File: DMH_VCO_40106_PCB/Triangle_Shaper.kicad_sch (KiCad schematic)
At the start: 16 parts, among them Q3 BC548, Q4 BC548, U3 TL074, U4 TL074

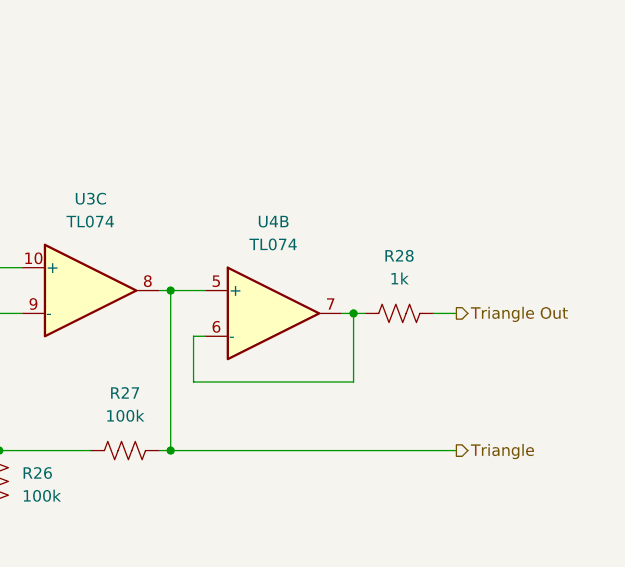
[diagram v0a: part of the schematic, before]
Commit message: Started positioning components on PCB
Moving some input resistores from main PCB to Jacks PCB
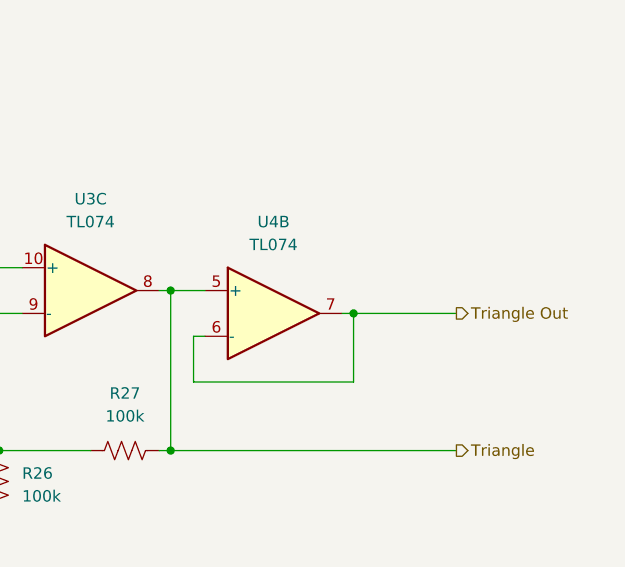
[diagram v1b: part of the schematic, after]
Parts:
- removed R28: 1k, Resistor_THT:R_Axial_DIN0204_L3.6mm_D1.6mm_P5.08mm_Horizontal, symbol Device:R_US
- C12: footprint (none) -> Capacitor_THT:C_Disc_D3.0mm_W2.0mm_P2.50mm
- C13: footprint (none) -> Capacitor_THT:C_Disc_D4.3mm_W1.9mm_P5.00mm
- Q3, Q4: footprint Package_TO_SOT_THT:TO-92_Inline -> Package_TO_SOT_THT:TO-92_Inline_Wide
- R22, R23, R24, R25, R26, R27: footprint Resistor_THT:R_Axial_DIN0204_L3.6mm_D1.6mm_P5.08mm_Horizontal -> Resistor_THT:R_Axial_DIN0207_L6.3mm_D2.5mm_P7.62mm_Horizontal
- TP5, TP6: footprint (none) -> TestPoint:TestPoint_THTPad_2.0x2.0mm_Drill1.0mm; now left out of the parts list
- U4: footprint (none) -> Package_DIP:DIP-14_W7.62mm_Socket
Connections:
- net Triangle Out: now also U4.6 (-), U4.7
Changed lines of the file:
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@@
 	(wire
 		(pts
-			(xy 219.71 99.06) (xy 222.25 99.06)
+			(xy 210.82 99.06) (xy 222.25 99.06)
 		)
 		(stroke
@@
 		)
 	)
-	(wire
-		(pts
-			(xy 210.82 99.06) (xy 212.09 99.06)
-		)
-		(stroke
-			(width 0)
-			(type default)
-		)
-	)
 	(hierarchical_label "Triangle Out"
 		(shape output)
@@
 			)
 		)
-		(property "Footprint" "Resistor_THT:R_Axial_DIN0204_L3.6mm_D1.6mm_P5.08mm_Horizontal"
+		(property "Footprint" "Resistor_THT:R_Axial_DIN0207_L6.3mm_D2.5mm_P7.62mm_Horizontal"
 			(at 143.764 99.314 90)
 			(effects
@@
 			)
 		)
-		(property "Footprint" "Resistor_THT:R_Axial_DIN0204_L3.6mm_D1.6mm_P5.08mm_Horizontal"
+		(property "Footprint" "Resistor_THT:R_Axial_DIN0207_L6.3mm_D2.5mm_P7.62mm_Horizontal"
 			(at 122.936 95.504 90)
 			(effects
@@
 			)
 		)
-		(property "Footprint" "Resistor_THT:R_Axial_DIN0204_L3.6mm_D1.6mm_P5.08mm_Horizontal"
+		(property "Footprint" "Resistor_THT:R_Axial_DIN0207_L6.3mm_D2.5mm_P7.62mm_Horizontal"
 			(at 185.674 113.284 90)
 			(effects
@@
 			)
 		)
-		(property "Footprint" "Resistor_THT:R_Axial_DIN0204_L3.6mm_D1.6mm_P5.08mm_Horizontal"
+		(property "Footprint" "Resistor_THT:R_Axial_DIN0207_L6.3mm_D2.5mm_P7.62mm_Horizontal"
 			(at 172.466 118.364 90)
 			(effects
@@
 		(unit 1)
 		(exclude_from_sim no)
-		(in_bom yes)
-		(on_board yes)
+		(in_bom no)
+		(on_board no)
 		(dnp no)
 		(fields_autoplaced yes)
@@
 			)
 		)
-		(property "Footprint" ""
+		(property "Footprint" "TestPoint:TestPoint_THTPad_2.0x2.0mm_Drill1.0mm"
 			(at 140.97 88.9 0)
 			(effects
@@
 			)
 		)
+		(property "Function" ""
+			(at 135.89 88.9 0)
+			(effects
+				(font
+					(size 1.27 1.27)
+				)
+				(hide yes)
+			)
+		)
 		(pin "1"
 		)
@@
 				(path "/fefed352-c100-4617-bbfb-c55e7427b122/0e77ed5b-450a-412c-a492-589f053c9c73"
 					(reference "TP5")
-					(unit 1)
-				)
-			)
-		)
-	)
-	(symbol
-		(lib_id "Device:R_US")
-		(at 215.9 99.06 90)
-		(unit 1)
-		(exclude_from_sim no)
-		(in_bom yes)
-		(on_board yes)
-		(dnp no)
-		(fields_autoplaced yes)
-		(property "Reference" "R28"
-			(at 215.9 92.71 90)
-			(effects
-				(font
-					(size 1.27 1.27)
-				)
-			)
-		)
-		(property "Value" "1k"
-			(at 215.9 95.25 90)
-			(effects
-				(font
-					(size 1.27 1.27)
-				)
-			)
-		)
-		(property "Footprint" "Resistor_THT:R_Axial_DIN0204_L3.6mm_D1.6mm_P5.08mm_Horizontal"
-			(at 216.154 98.044 90)
-			(effects
-				(font
-					(size 1.27 1.27)
-				)
-				(hide yes)
-			)
-		)
-		(property "Datasheet" "~"
-			(at 215.9 99.06 0)
-			(effects
-				(font
-					(size 1.27 1.27)
-				)
-				(hide yes)
-			)
-		)
-		(property "Description" "Resistor, US symbol"
-			(at 215.9 99.06 0)
-			(effects
-				(font
-					(size 1.27 1.27)
-				)
-				(hide yes)
-			)
-		)
-		(pin "2"
-		)
-		(pin "1"
-		)
-		(instances
-			(project "VCO mki PCB"
-				(path "/fefed352-c100-4617-bbfb-c55e7427b122/0e77ed5b-450a-412c-a492-589f053c9c73"
-					(reference "R28")
 					(unit 1)
 				)
@@
 			)
 		)
-		(property "Footprint" ""
+		(property "Footprint" "Package_DIP:DIP-14_W7.62mm_Socket"
 			(at 200.66 96.52 0)
 			(effects
@@
 			)
 		)
+		(property "Function" ""
+			(at 201.93 99.06 0)
+			(effects
+				(font
+					(size 1.27 1.27)
+				)
+				(hide yes)
+			)
+		)
 		(pin "3"
 		)
@@
 			)
 		)
-		(property "Footprint" "Package_TO_SOT_THT:TO-92_Inline"
+		(property "Footprint" "Package_TO_SOT_THT:TO-92_Inline_Wide"
 			(at 102.87 102.235 0)
 			(effects
@@
 			)
 		)
-		(property "Footprint" "Resistor_THT:R_Axial_DIN0204_L3.6mm_D1.6mm_P5.08mm_Horizontal"
+		(property "Footprint" "Resistor_THT:R_Axial_DIN0207_L6.3mm_D2.5mm_P7.62mm_Horizontal"
 			(at 163.576 108.204 90)
 			(effects
@@
 			)
 		)
-		(property "Footprint" ""
+		(property "Footprint" "Capacitor_THT:C_Disc_D3.0mm_W2.0mm_P2.50mm"
 			(at 148.8948 104.14 0)
 			(effects
@@
 			)
 		)
-		(property "Footprint" "Resistor_THT:R_Axial_DIN0204_L3.6mm_D1.6mm_P5.08mm_Horizontal"
+		(property "Footprint" "Resistor_THT:R_Axial_DIN0207_L6.3mm_D2.5mm_P7.62mm_Horizontal"
 			(at 122.936 118.364 90)
 			(effects
@@
 		(unit 1)
 		(exclude_from_sim no)
-		(in_bom yes)
-		(on_board yes)
+		(in_bom no)
+		(on_board no)
 		(dnp no)
 		(fields_autoplaced yes)
@@
 			)
 		)
-		(property "Footprint" ""
+		(property "Footprint" "TestPoint:TestPoint_THTPad_2.0x2.0mm_Drill1.0mm"
 			(at 154.94 88.9 0)
 			(effects
@@
 			)
 		)
+		(property "Function" ""
+			(at 149.86 88.9 0)
+			(effects
+				(font
+					(size 1.27 1.27)
+				)
+				(hide yes)
+			)
+		)
 		(pin "1"
 		)
@@
 			)
 		)
-		(property "Footprint" ""
+		(property "Footprint" "Capacitor_THT:C_Disc_D4.3mm_W1.9mm_P5.00mm"
 			(at 160.02 99.3648 0)
 			(effects
@@
 			)
 		)
-		(property "Footprint" "Package_TO_SOT_THT:TO-92_Inline"
+		(property "Footprint" "Package_TO_SOT_THT:TO-92_Inline_Wide"
 			(at 124.46 108.585 0)
 			(effects

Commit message: Component placement ongoing
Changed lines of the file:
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@@
+		)
+	)
+	(text_box "Moved R28=1k to Inputs and Outputs sheet"
+		(exclude_from_sim no)
+		(at 212.09 90.17 0)
+		(size 17.78 7.62)
+		(stroke
+			(width 0)
+			(type default)
+		)
+		(fill
+			(type none)
+		)
+		(effects
+			(font
+				(size 1.27 1.27)
+			)
+			(justify left)
 		)
 	)

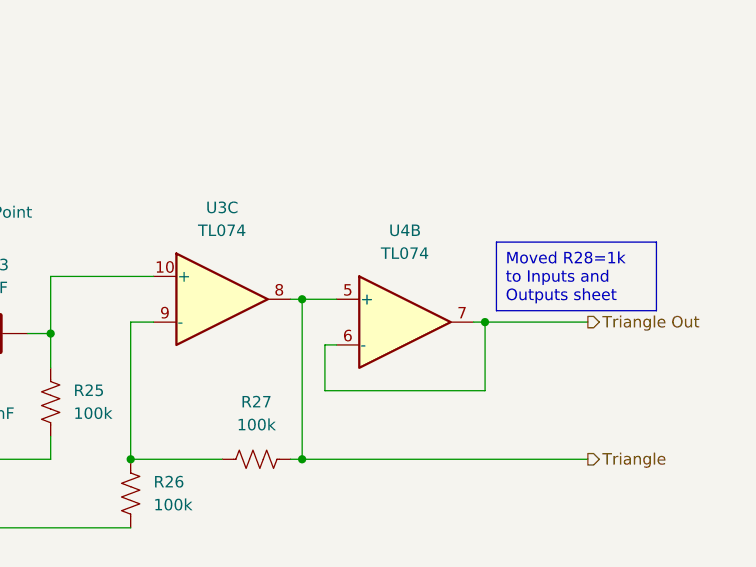
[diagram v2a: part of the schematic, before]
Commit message: Organized Square and Sine Shaper components
Also re-annotated the TL074 ICs to improve the layout
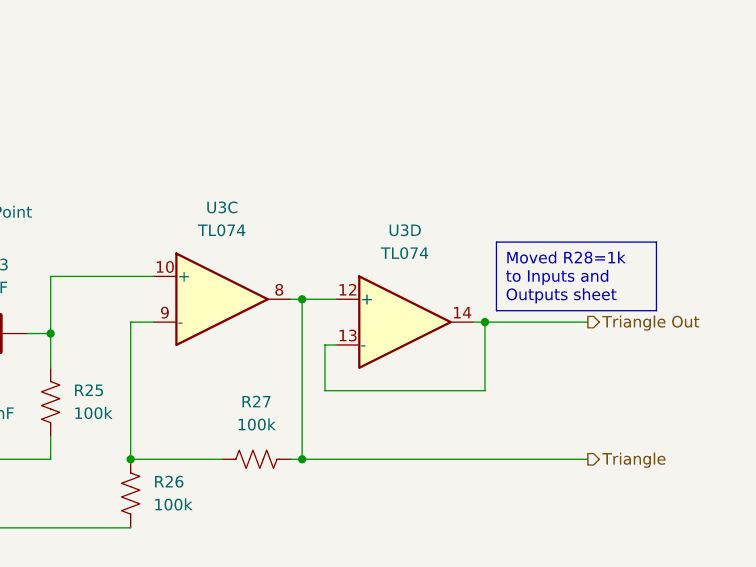
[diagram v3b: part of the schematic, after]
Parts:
- renumbered U4 to U3
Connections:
- net Triangle: now also U3.12 (+); no longer U3.5 (+)
- net Triangle Out: now also U3.13 (-), U3.14; no longer U3.6 (-), U3.7
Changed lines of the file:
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@@
+			)
+		)
+		(property "Function" ""
+			(at 181.61 96.52 0)
+			(effects
+				(font
+					(size 1.27 1.27)
+				)
+				(hide yes)
 			)
 		)
@@
 		(lib_id "Amplifier_Operational:TL074")
 		(at 201.93 99.06 0)
-		(unit 2)
+		(unit 4)
 		(exclude_from_sim no)
 		(in_bom yes)
@@
 		(dnp no)
 		(fields_autoplaced yes)
-		(property "Reference" "U4"
+		(property "Reference" "U3"
 			(at 201.93 88.9 0)
 			(effects
@@
 			(project ""
 				(path "/fefed352-c100-4617-bbfb-c55e7427b122/0e77ed5b-450a-412c-a492-589f053c9c73"
-					(reference "U4")
-					(unit 2)
-				)
-			)
+					(reference "U3")
+					(unit 4)
+				)
+			)

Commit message: Finished physical placement
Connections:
- net Triangle: now also U3.1, U3.5 (+); no longer U3.12 (+), U3.8
- net Triangle Out: now also U3.6 (-), U3.7; no longer U3.13 (-), U3.14
- net at C13.2, R25.1: now also U3.3 (+); no longer U3.10 (+)
- net at R26.1, R27.1: now also U3.2 (-); no longer U3.9 (-)
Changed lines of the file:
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@@
 		(lib_id "Amplifier_Operational:TL074")
 		(at 181.61 96.52 0)
-		(unit 3)
+		(unit 1)
 		(exclude_from_sim no)
 		(in_bom yes)
@@
 				(path "/fefed352-c100-4617-bbfb-c55e7427b122/0e77ed5b-450a-412c-a492-589f053c9c73"
 					(reference "U3")
-					(unit 3)
+					(unit 1)
 				)
 			)
@@
 		(lib_id "Amplifier_Operational:TL074")
 		(at 201.93 99.06 0)
-		(unit 4)
+		(unit 2)
 		(exclude_from_sim no)
 		(in_bom yes)
@@
 				(path "/fefed352-c100-4617-bbfb-c55e7427b122/0e77ed5b-450a-412c-a492-589f053c9c73"
 					(reference "U3")
-					(unit 4)
-				)
-			)
+					(unit 2)
+				)
+			)

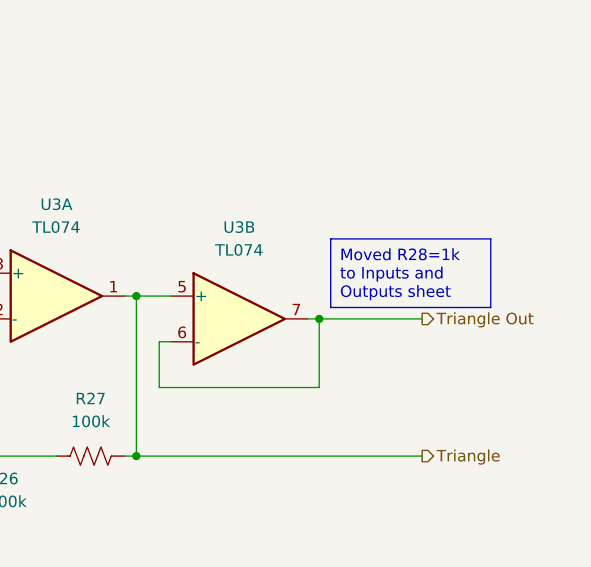
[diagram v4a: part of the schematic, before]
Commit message: Placed input and output resistors back in main PCB
This ensures a more clear schematic and leaves the Connectors PCB only with actual connectors.
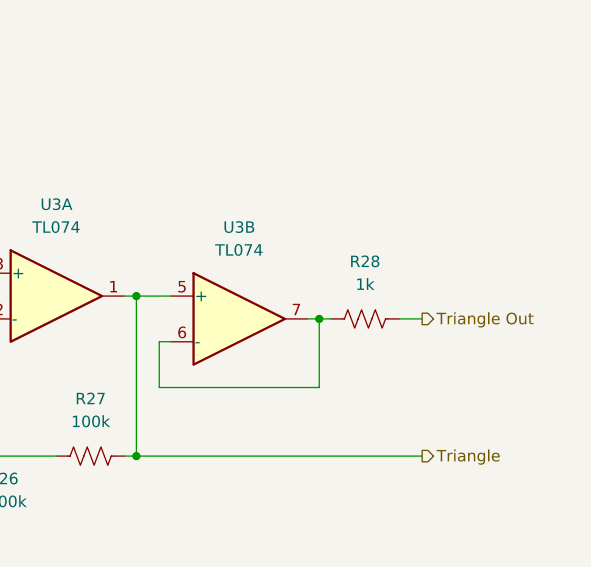
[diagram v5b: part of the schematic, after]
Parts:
- added R28: 1k, Resistor_THT:R_Axial_DIN0207_L6.3mm_D2.5mm_P7.62mm_Horizontal, symbol Device:R_US
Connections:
- net Triangle Out: now also R28.1; no longer U3.6 (-), U3.7
- new net: R28.2, U3.6 (-), U3.7
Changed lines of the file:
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@@
+	(wire
+		(pts
+			(xy 219.71 99.06) (xy 222.25 99.06)
+		)
+		(stroke
+			(width 0)
+			(type default)
+		)
+	)
 	(wire
 		(pts
@@
 	(wire
 		(pts
-			(xy 210.82 99.06) (xy 222.25 99.06)
-		)
-		(stroke
-			(width 0)
-			(type default)
-		)
-	)
-	(text_box "Moved R28=1k to Inputs and Outputs sheet"
-		(exclude_from_sim no)
-		(at 212.09 90.17 0)
-		(size 17.78 7.62)
-		(stroke
-			(width 0)
-			(type default)
-		)
-		(fill
-			(type none)
-		)
-		(effects
-			(font
-				(size 1.27 1.27)
-			)
-			(justify left)
+			(xy 210.82 99.06) (xy 212.09 99.06)
+		)
+		(stroke
+			(width 0)
+			(type default)
 		)
 	)
@@
 					(unit 1)
 				)
+			)
+		)
+	)
+	(symbol
+		(lib_id "Device:R_US")
+		(at 215.9 99.06 270)
+		(unit 1)
+		(exclude_from_sim no)
+		(in_bom yes)
+		(on_board yes)
+		(dnp no)
+		(fields_autoplaced yes)
+		(property "Reference" "R28"
+			(at 215.9 92.71 90)
+			(effects
+				(font
+					(size 1.27 1.27)
+				)
+			)
+		)
+		(property "Value" "1k"
+			(at 215.9 95.25 90)
+			(effects
+				(font
+					(size 1.27 1.27)
+				)
+			)
+		)
+		(property "Footprint" "Resistor_THT:R_Axial_DIN0207_L6.3mm_D2.5mm_P7.62mm_Horizontal"
+			(at 215.646 100.076 90)
+			(effects
+				(font
+					(size 1.27 1.27)
+				)
+				(hide yes)
+			)
+		)
+		(property "Datasheet" "~"
+			(at 215.9 99.06 0)
+			(effects
+				(font
+					(size 1.27 1.27)
+				)
+				(hide yes)
+			)
+		)
+		(property "Description" "Resistor, US symbol"
+			(at 215.9 99.06 0)
+			(effects
+				(font
+					(size 1.27 1.27)
+				)
+				(hide yes)
+			)
+		)
+		(pin "2"
+		)
+		(pin "1"
+		)
+		(instances
+			(project "DMH_VCO_40106_PCB"
+				(path "/fefed352-c100-4617-bbfb-c55e7427b122/0e77ed5b-450a-412c-a492-589f053c9c73"
+					(reference "R28")
+					(unit 1)
+				)

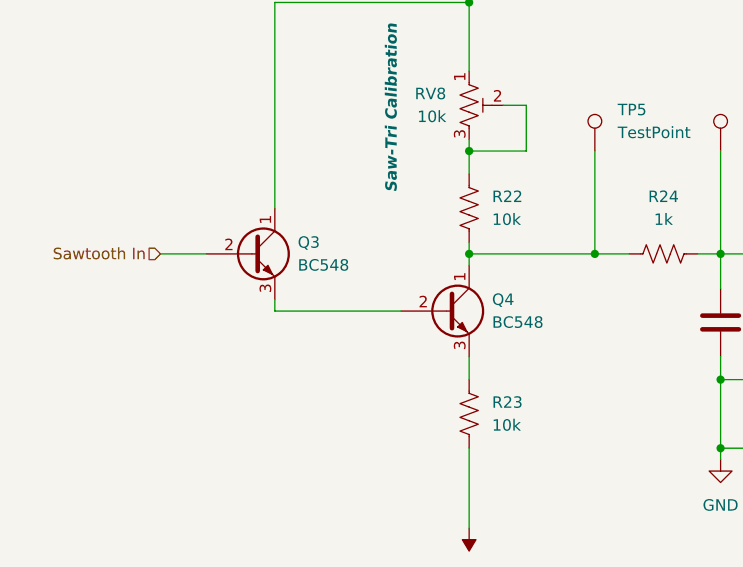
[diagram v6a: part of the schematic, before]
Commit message: Changed buffer resistor to 10M
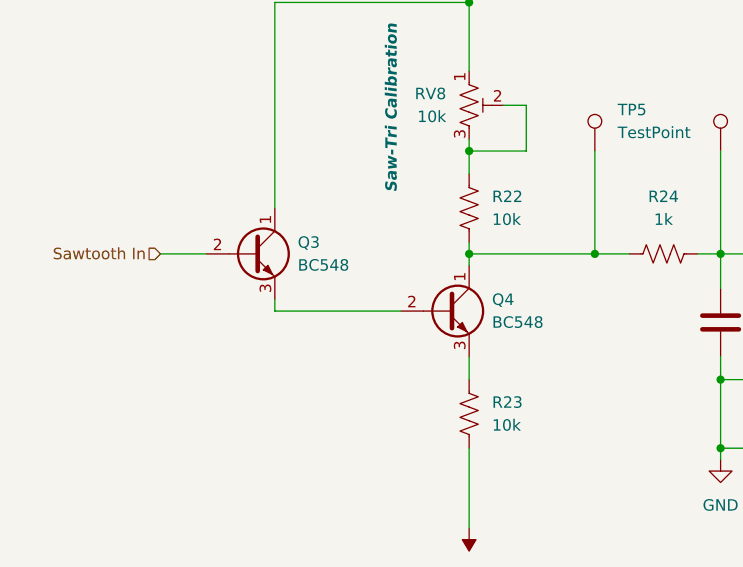
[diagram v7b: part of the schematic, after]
